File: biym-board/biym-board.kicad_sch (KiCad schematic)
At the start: 0 parts

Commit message: Add some datasheets
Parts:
- added FW?: FEATHERWING_nRF52_PIN_RECEPTACLES, Janelia:FEATHERWING_PIN_RECEPTACLES, symbol janelia:FEATHERWING_nRF52_PIN_RECEPTACLES
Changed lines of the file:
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@@
   (title_block
     (title "biym-board")
-    (date "2022-10-29")
+    (date "2022-11-08")
     (rev "0.1")
     (company "Peter Polidoro")
+  )
+  (symbol (lib_id "janelia:FEATHERWING_nRF52_PIN_RECEPTACLES") (at 71.12 106.68 0) (unit 1)
+    (in_bom yes) (on_board yes)
+    (property "Reference" "FW?" (id 0) (at 85.09 81.28 0))
+    (property "Value" "FEATHERWING_nRF52_PIN_RECEPTACLES" (id 1) (at 71.12 132.08 0))
+    (property "Footprint" "Janelia:FEATHERWING_PIN_RECEPTACLES" (id 2) (at 71.12 72.39 0)
+      (effects (font (size 1.27 1.27)) hide)
+    )
+    (property "Datasheet" "" (id 3) (at 54.61 82.55 90)
+      (effects (font (size 1.27 1.27)) hide)
+    )
+    (property "Vendor" "Digi-Key" (id 4) (at 71.12 77.47 0)
+      (effects (font (size 1.524 1.524)) hide)
+    )
+    (property "Vendor Part Number" "ED90331-ND" (id 5) (at 71.12 74.93 0)
+      (effects (font (size 1.524 1.524)) hide)
+    )
+    (property "Description" "CONN PIN RCPT .025-.037 SOLDER" (id 6) (at 71.12 72.39 0)
+      (effects (font (size 1.524 1.524)) hide)
+    )
+    (property "Quantity" "28" (id 7) (at 71.12 106.68 0)
+      (effects (font (size 1.27 1.27)) hide)
+    )
+    (property "Manufacturer" "Mill-Max Manufacturing Corp." (id 8) (at 71.12 106.68 0)
+      (effects (font (size 1.27 1.27)) hide)
+    )
+    (property "Manufacturer Part Number" "0305-0-15-15-47-27-10-0" (id 9) (at 71.12 106.68 0)
+      (effects (font (size 1.27 1.27)) hide)
+    )
+    (pin "1")
+    (pin "10")
+    (pin "11")
+    (pin "12")
+    (pin "13")
+    (pin "14")
+    (pin "15")
+    (pin "16")
+    (pin "17")
+    (pin "18")
+    (pin "19")
+    (pin "2")
+    (pin "20")
+    (pin "21")
+    (pin "22")
+    (pin "23")
+    (pin "24")
+    (pin "25")
+    (pin "26")
+    (pin "27")
+    (pin "28")
+    (pin "3")
+    (pin "4")
+    (pin "5")
+    (pin "6")
+    (pin "7")
+    (pin "8")
+    (pin "9")
   )
   (sheet_instances
     (path "/" (page "1"))
   )
+  (symbol_instances
+    (path "/362b0466-0e34-4ef2-87f7-57577a17fdd4"
+      (reference "FW?") (unit 1) (value "FEATHERWING_nRF52_PIN_RECEPTACLES") (footprint "Janelia:FEATHERWING_PIN_RECEPTACLES")
+    )
+  )
 )

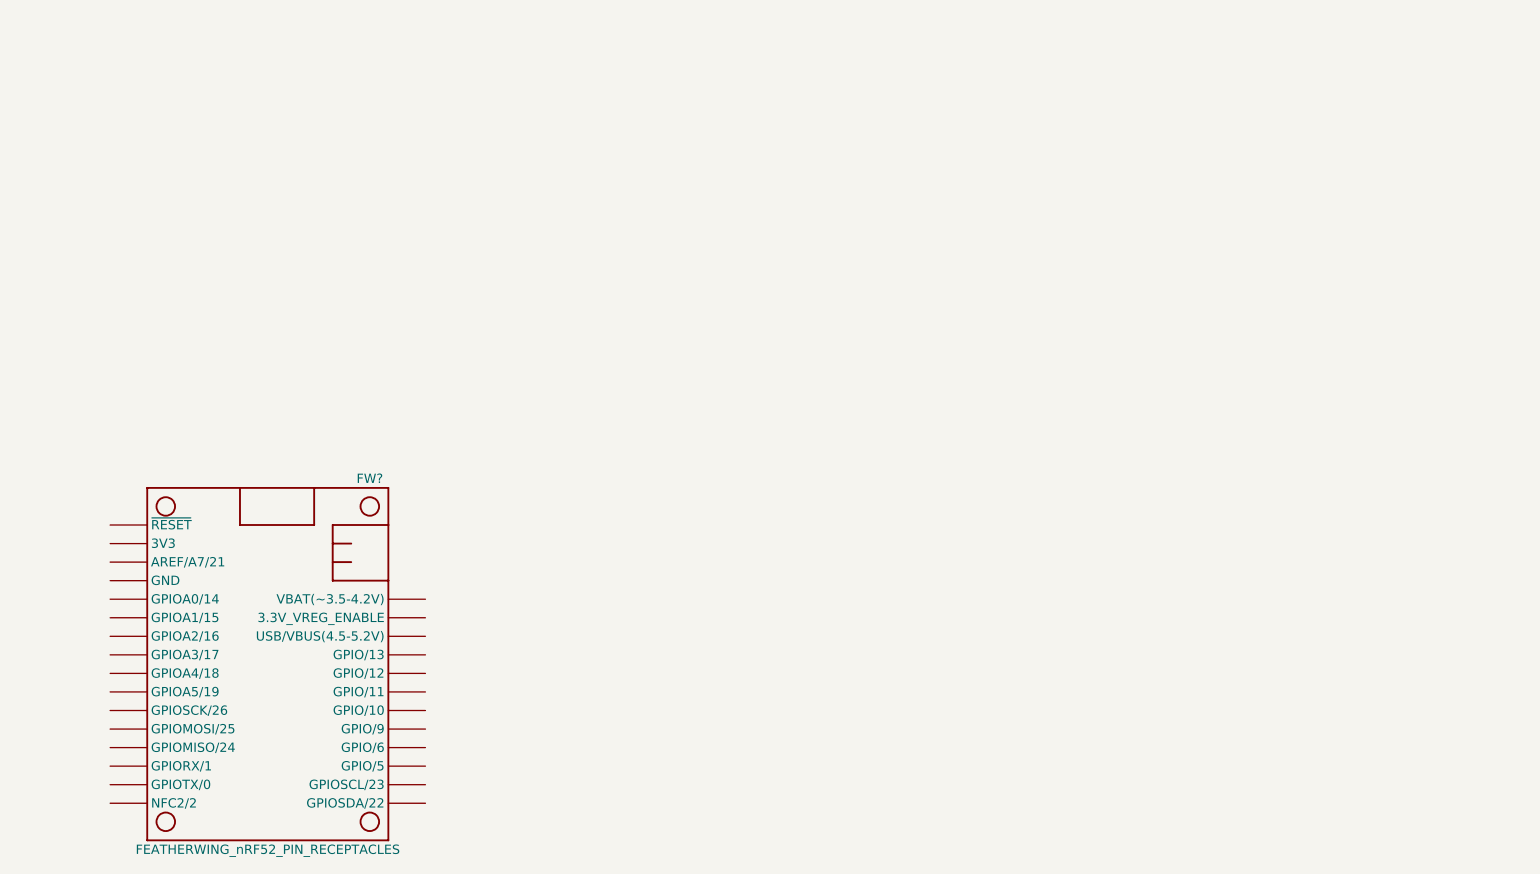
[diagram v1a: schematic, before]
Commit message: Add power stage
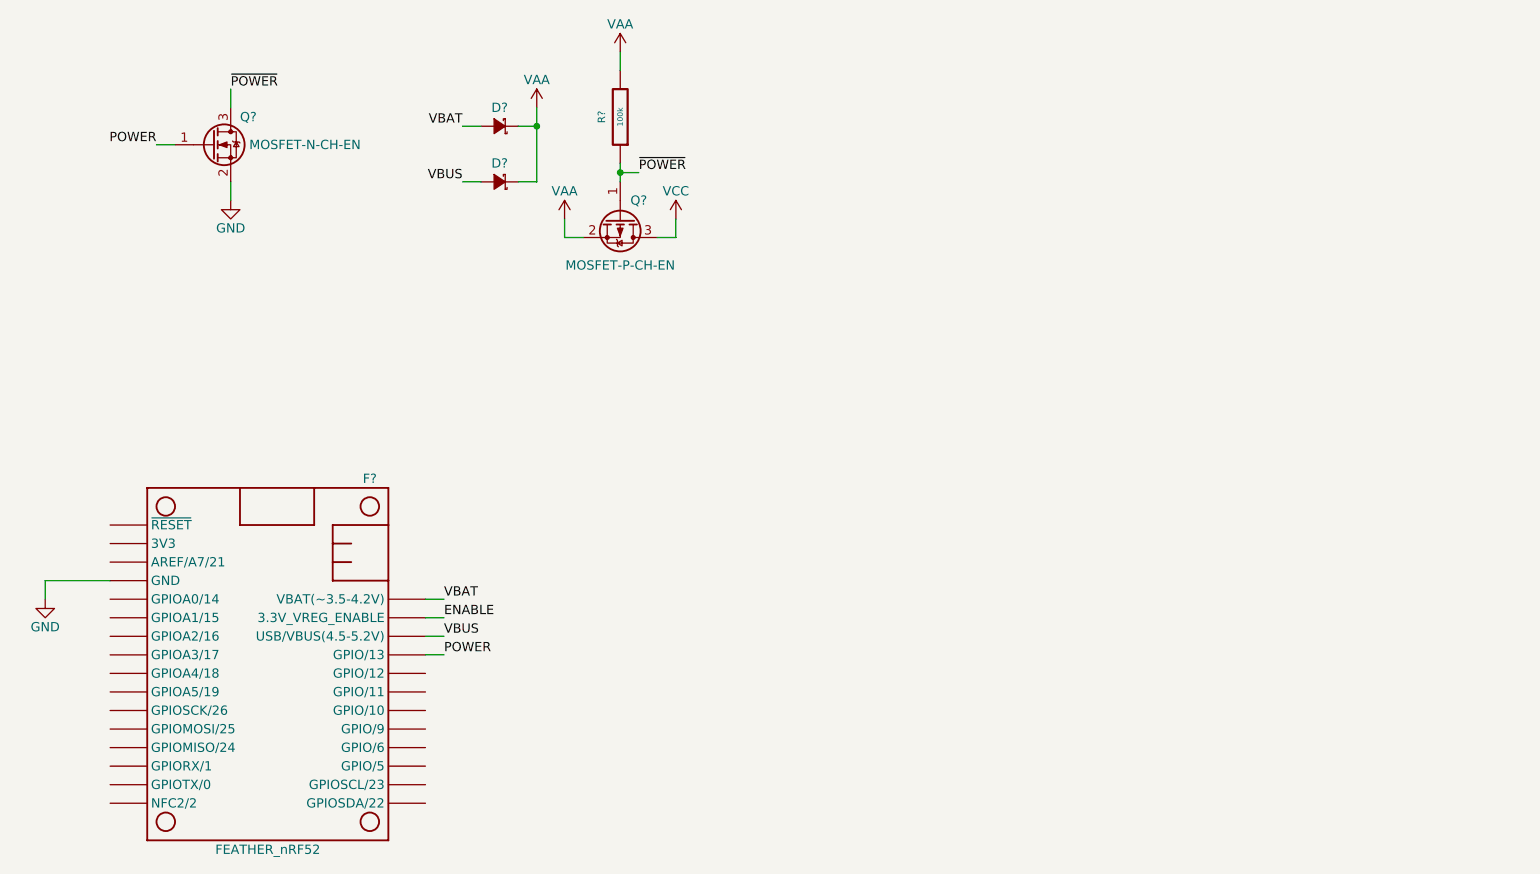
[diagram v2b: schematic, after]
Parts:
- added D? (x2): DIODE_SCHOTTKY_15V_1A, footprints:DO-214BA, symbol Janelia:DIODE_SCHOTTKY_15V_1A
- added Q?: MOSFET-P-CH-EN, Janelia:SOT-23-3, symbol Janelia:MOSFET-P-CH-EN-DMP2045UQ-7
- added Q?: MOSFET-N-CH-EN, Janelia:SOT-23-3, symbol Janelia:MOSFET-N-CH-EN-DMG2302UKQ-7
- added R?: 100k, footprints:SM0402, symbol Janelia:100k_0402
- F?: renamed from FW?; value FEATHERWING_nRF52_PIN_RECEPTACLES -> FEATHER_nRF52
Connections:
- net POWER: now reaches F?.25 (GPIO/13)
- net POWER: now also Q?.1 (G)
- net VBUS: now reaches F?.26 (USB/VBUS(4.5-5.2V))
- net VBUS: now also D?.2 (A)
- net ENABLE: now reaches F?.27 (3.3V_VREG_ENABLE)
- net VBAT: now reaches F?.28 (VBAT(~3.5-4.2V))
- net VBAT: now also D?.2 (A)
- net GND: now reaches F?.4 (GND)
- net GND: now also Q?.2 (S)
- new net VAA: D?.1 (K), D?.1 (K), Q?.2 (S), R?.2
- new net VCC: Q?.3 (D)
- new net ~{POWER}: Q?.1 (G), Q?.3 (D), R?.1

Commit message: Add power
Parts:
- removed D? (x2): DIODE_SCHOTTKY_15V_1A, footprints:DO-214BA, symbol Janelia:DIODE_SCHOTTKY_15V_1A
- removed F?: FEATHER_nRF52, Janelia:FEATHERWING_PIN_RECEPTACLES, symbol janelia:FEATHERWING_nRF52_PIN_RECEPTACLES
- removed Q?: MOSFET-P-CH-EN, Janelia:SOT-23-3, symbol Janelia:MOSFET-P-CH-EN-DMP2045UQ-7
- removed Q?: MOSFET-N-CH-EN, Janelia:SOT-23-3, symbol Janelia:MOSFET-N-CH-EN-DMG2302UKQ-7
- removed R?: 100k, footprints:SM0402, symbol Janelia:100k_0402
- added FW1: FEATHERWING_nRF52_PIN_RECEPTACLES, Janelia:FEATHERWING_PIN_RECEPTACLES, symbol Janelia:FEATHERWING_nRF52_PIN_RECEPTACLES
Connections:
- net GND: now also FW1.4 (GND)
- net VBAT: now also FW1.28 (VBAT(~3.5-4.2V))
- new net ENABLE_HIGH_VOLTAGE: FW1.25 (GPIO/13)
- new net ENABLE_LOW_VOLTAGE: FW1.27 (3.3V_VREG_ENABLE)
- new net VUSB: FW1.26 (USB/VBUS(4.5-5.2V))
- no-connect marks 0 -> 24
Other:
- added sheet power (power.kicad_sch)

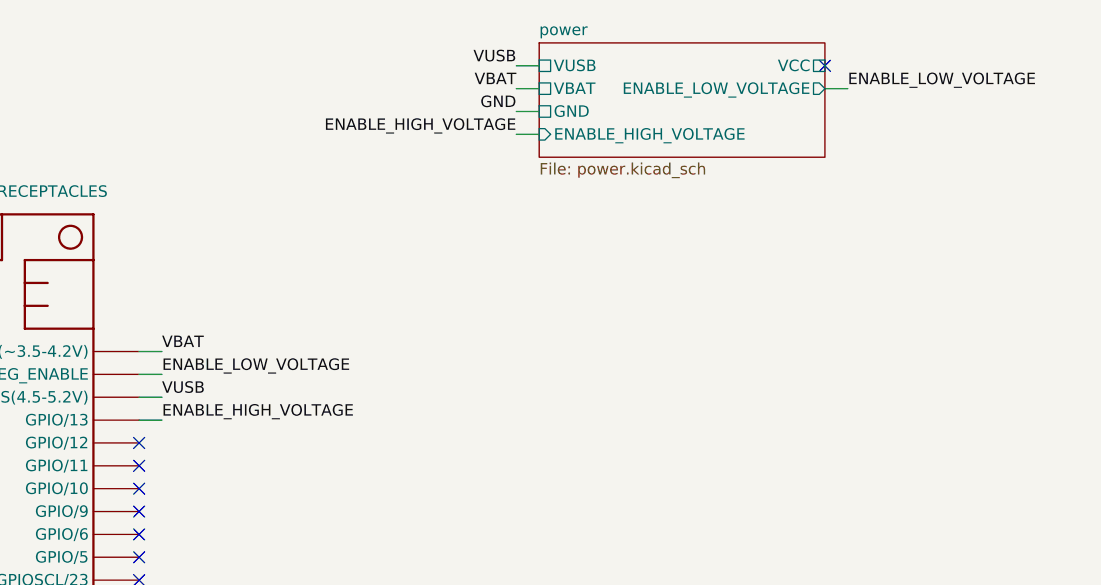
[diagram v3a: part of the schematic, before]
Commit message: Change diodes
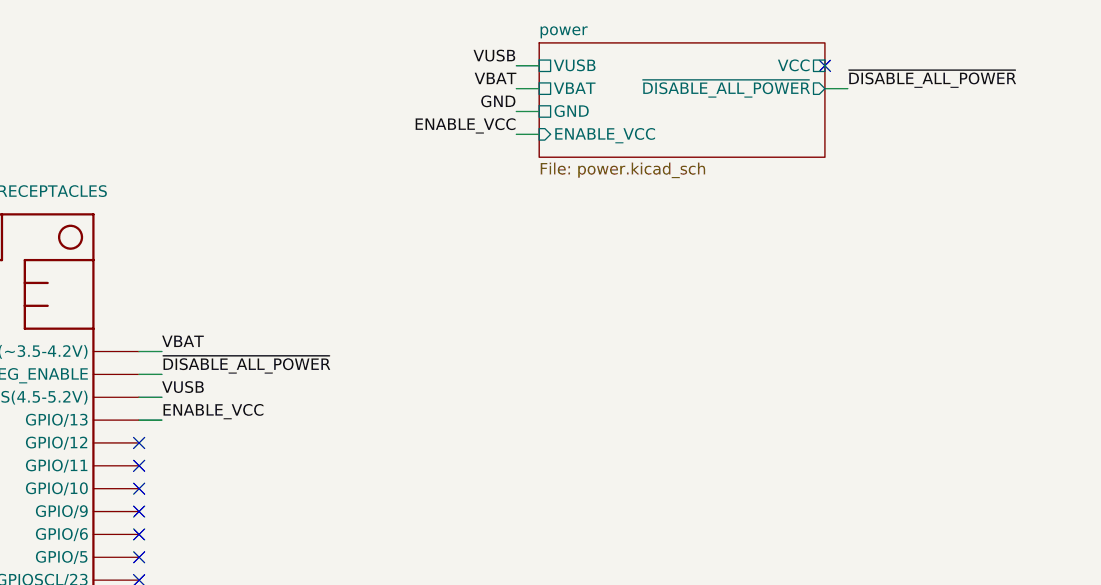
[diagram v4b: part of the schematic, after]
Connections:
- net ENABLE_HIGH_VOLTAGE renamed ENABLE_VCC
- net ENABLE_LOW_VOLTAGE renamed ~{DISABLE_ALL_POWER}
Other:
- sheet power ports: added ENABLE_VCC, ~{DISABLE_ALL_POWER}; removed ENABLE_HIGH_VOLTAGE, ENABLE_LOW_VOLTAGE
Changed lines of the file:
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@@
   (title_block
     (title "biym-board")
-    (date "2022-11-08")
+    (date "2022-11-10")
     (rev "0.1")
     (company "Peter Polidoro")
@@
     (stroke (width 0) (type default) (color 0 0 0 0))
   )
-  (label "ENABLE_HIGH_VOLTAGE" (at 95.25 105.41 0)
+  (label "ENABLE_VCC" (at 95.25 105.41 0)
     (effects (font (size 1.27 1.27)) (justify left bottom))
   )
@@
     (effects (font (size 1.27 1.27)) (justify right bottom))
   )
-  (label "ENABLE_HIGH_VOLTAGE" (at 134.62 73.66 180)
+  (label "ENABLE_VCC" (at 134.62 73.66 180)
     (effects (font (size 1.27 1.27)) (justify right bottom))
   )
@@
     (effects (font (size 1.27 1.27)) (justify left bottom))
   )
-  (label "ENABLE_LOW_VOLTAGE" (at 171.45 68.58 0)
-    (effects (font (size 1.27 1.27)) (justify left bottom))
-  )
-  (label "ENABLE_LOW_VOLTAGE" (at 95.25 100.33 0)
+  (label "~{DISABLE_ALL_POWER}" (at 171.45 68.58 0)
+    (effects (font (size 1.27 1.27)) (justify left bottom))
+  )
+  (label "~{DISABLE_ALL_POWER}" (at 95.25 100.33 0)
     (effects (font (size 1.27 1.27)) (justify left bottom))
   )
@@
       (effects (font (size 1.27 1.27)) (justify left))
     )
-    (pin "ENABLE_HIGH_VOLTAGE" input (at 137.16 73.66 180)
-      (effects (font (size 1.27 1.27)) (justify left))
-    )
-    (pin "ENABLE_LOW_VOLTAGE" output (at 168.91 68.58 0)
+    (pin "~{DISABLE_ALL_POWER}" output (at 168.91 68.58 0)
       (effects (font (size 1.27 1.27)) (justify right))
+    )
+    (pin "ENABLE_VCC" input (at 137.16 73.66 180)
+      (effects (font (size 1.27 1.27)) (justify left))
     )
   )
@@
   )
   (symbol_instances
-    (path "/2c398cb1-cb17-49ba-86d6-22731656ead9/d2cbfbee-bcfb-4ed9-b3fa-540be86c6c52"
-      (reference "D1") (unit 1) (value "DIODE_SCHOTTKY_15V_1A") (footprint "footprints:DO-214BA")
-    )
-    (path "/2c398cb1-cb17-49ba-86d6-22731656ead9/f78441dc-9d0d-4d39-aaa8-49619bc8e2d4"
-      (reference "D2") (unit 1) (value "DIODE_SCHOTTKY_15V_1A") (footprint "footprints:DO-214BA")
+    (path "/2c398cb1-cb17-49ba-86d6-22731656ead9/ae7d77aa-4639-4a04-8768-f2282fb5051c"
+      (reference "D1") (unit 1) (value "DIODE_SCHOTTKY_40V_2A_0603") (footprint "Janelia:SM0603_DSN2")
+    )
+    (path "/2c398cb1-cb17-49ba-86d6-22731656ead9/7ddeef5d-5855-4b75-a2bc-b5412afa8482"
+      (reference "D2") (unit 1) (value "DIODE_SCHOTTKY_40V_2A_0603") (footprint "Janelia:SM0603_DSN2")
     )
     (path "/55a2d7cd-47d7-49c1-94ac-5e60fd064dcf"
       (reference "FW1") (unit 1) (value "FEATHERWING_nRF52_PIN_RECEPTACLES") (footprint "Janelia:FEATHERWING_PIN_RECEPTACLES")
     )
-    (path "/2c398cb1-cb17-49ba-86d6-22731656ead9/6c21a8d5-bff4-440f-baad-391d3359c849"
+    (path "/2c398cb1-cb17-49ba-86d6-22731656ead9/ee181020-0a66-4e94-8afa-04e718523ff4"
       (reference "J1") (unit 1) (value "JST_SH_BM02_VERTICAL") (footprint "Janelia:JST_SH_BM02B-SRSS-TB_1x02-1MP_P1.00mm_Vertical")
     )
@@
     )
     (path "/2c398cb1-cb17-49ba-86d6-22731656ead9/1c5e1e5d-544e-4c6a-8063-3a626f207568"
-      (reference "R1") (unit 1) (value "100k") (footprint "footprints:SM0402")
-    )
-  )
+      (reference "R1") (unit 1) (value "100k") (footprint "Janelia:SM0402")
+    )
+  )
